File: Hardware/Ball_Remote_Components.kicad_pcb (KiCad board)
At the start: 4 copper layers, 75 x 75 mm, 55 parts, among them J1 I2C_Gyro_Module, J2 USB_B_Micro, J3 SWD_Header, Q1 SI2333DS, SW1 SW_SPDT, U1 MCP73831-2-OT, U2 L3GD20, U3 STM32WB35, U4 LD3985M28R_SOT23, Y1 32MHz, Y2 32.768MHz

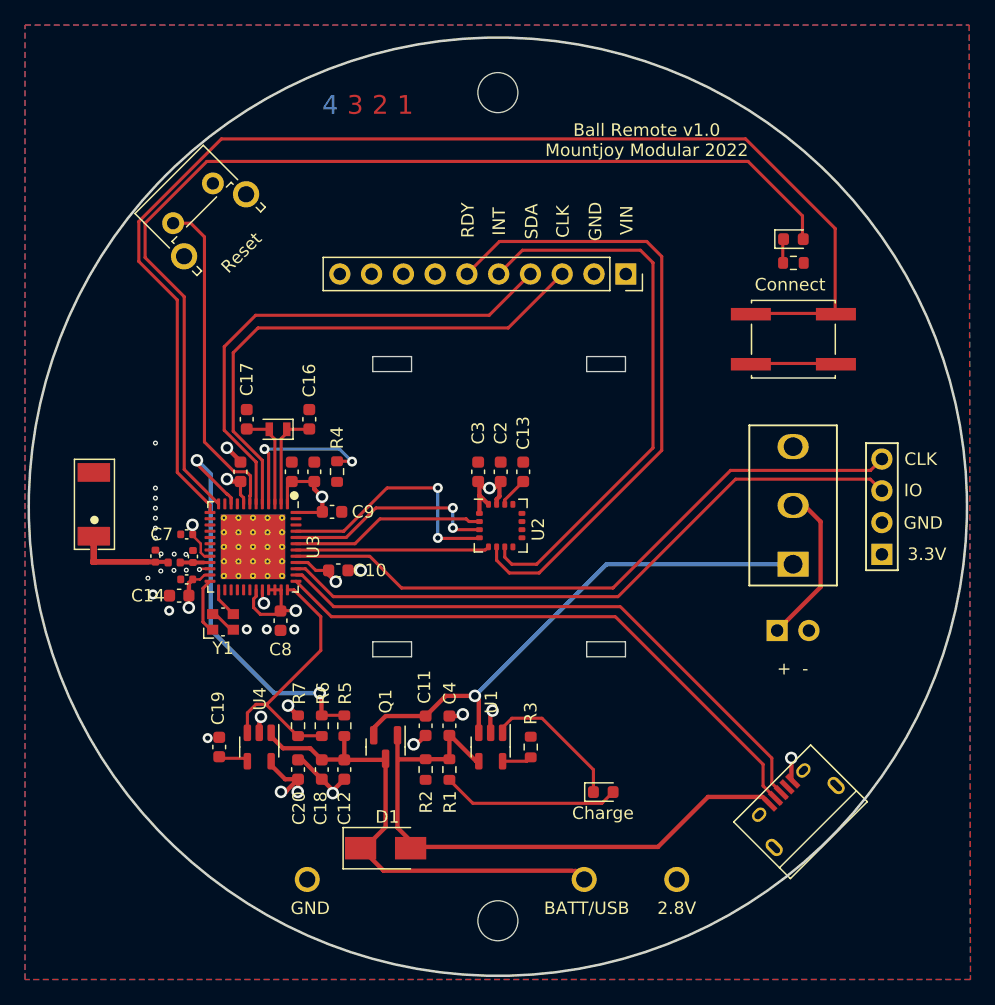
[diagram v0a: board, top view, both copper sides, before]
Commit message: More PCB clean-up
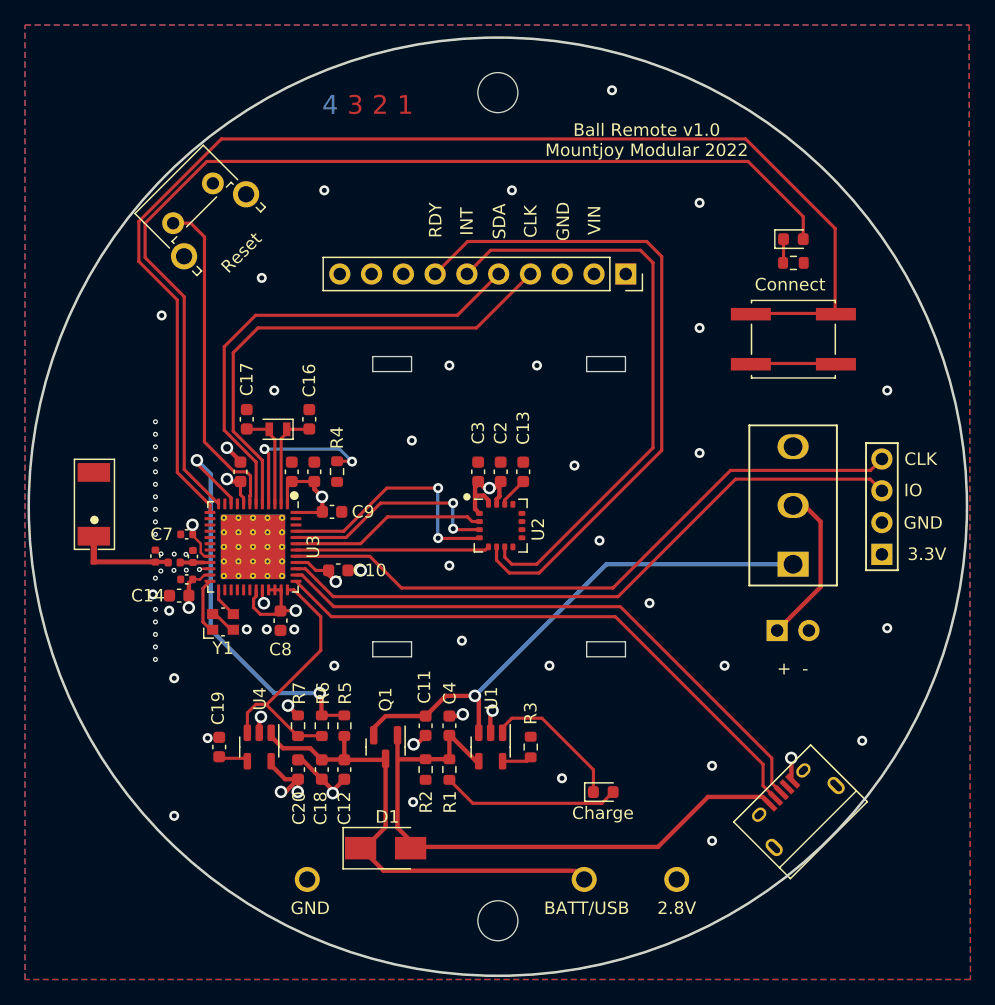
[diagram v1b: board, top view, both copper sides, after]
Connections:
- J1 pad 1: +2V8 -> unconnected-(J1-Pad1)
- J1 pad 2: GND -> +2V8
- J1 pad 3: /I2C_CLK -> GND
- J1 pad 4: /12C_SDA -> /I2C_CLK
- J1 pad 5: /G_INT -> /12C_SDA
- J1 pad 6: /G_RDY -> /G_INT
- J1 pad 7: unconnected-(J1-Pad7) -> /G_RDY
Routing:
- net /I2C_CLK: track 41.9 -> 39.4 mm
- net /12C_SDA: track 40.5 -> 38.0 mm
- net /G_RDY: track 51.4 -> 53.9 mm
- net /G_INT: track 45.1 -> 47.6 mm
- net +2V8: track 43.8 -> 44.7 mm
- net /SPI_MISO: track 17.2 -> 17.9 mm
- net GND: vias 31 -> 68

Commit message: Preparation of Gerbers for manufacturing
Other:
- board text added: "Off"
- board text added: "On"
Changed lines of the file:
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@@
     (40 "Dwgs.User" user "User.Drawings")
     (41 "Cmts.User" user "User.Comments")
-    (42 "Eco1.User" user "User.Eco1")
-    (43 "Eco2.User" user "User.Eco2")
     (44 "Edge.Cuts" user)
     (45 "Margin" user)
@@
     (48 "B.Fab" user)
     (49 "F.Fab" user)
-    (50 "User.1" user)
-    (51 "User.2" user)
-    (52 "User.3" user)
-    (53 "User.4" user)
-    (54 "User.5" user)
-    (55 "User.6" user)
-    (56 "User.7" user)
-    (57 "User.8" user)
-    (58 "User.9" user)
   )
   (setup
@@
       (drillshape 0)
       (scaleselection 1)
-      (outputdirectory "Gerbers/Remote/")
+      (outputdirectory "Gerbers/Ball_Remote/")
     )
   )
@@
       (effects (font (size 0.5 0.5) (thickness 0.1)))
     )
+    (fp_line (start -1.7 -3.5) (end 11.1 -3.5) (layer "F.SilkS") (width 0.15))
     (fp_line (start -1.7 3.5) (end 11.1 3.5) (layer "F.SilkS") (width 0.15))
     (fp_line (start 11.1 -3.5) (end 11.1 3.5) (layer "F.SilkS") (width 0.15))
-    (fp_line (start -1.7 -3.5) (end 11.1 -3.5) (layer "F.SilkS") (width 0.15))
     (fp_line (start -1.7 -3.5) (end -1.7 3.5) (layer "F.SilkS") (width 0.15))
-    (fp_line (start 11.1 -3.5) (end 11.1 3.5) (layer "F.CrtYd") (width 0.05))
     (fp_line (start -1.7 -3.5) (end 11.1 -3.5) (layer "F.CrtYd") (width 0.05))
     (fp_line (start -1.7 3.5) (end -1.7 -3.5) (layer "F.CrtYd") (width 0.05))
+    (fp_line (start 11.1 -3.5) (end 11.1 3.5) (layer "F.CrtYd") (width 0.05))
     (fp_line (start 11.1 3.5) (end -1.7 3.5) (layer "F.CrtYd") (width 0.05))
     (fp_line (start -1.7 -3.5) (end 11.1 -3.5) (layer "F.Fab") (width 0.1))
@@
   (gr_circle (center 143.4 104.5) (end 143.623607 104.5) (layer "F.SilkS") (width 0.15) (fill solid))
   (gr_circle (center 129.6 104.4) (end 129.882843 104.4) (layer "F.SilkS") (width 0.15) (fill solid))
+  (gr_rect (start 157.1 114.6) (end 160.9 95.5) (layer "F.SilkS") (width 0.15) (fill none))
   (gr_rect (start 131.925 85.2875) (end 157.425 87.9875) (layer "Dwgs.User") (width 0.15) (fill none))
   (gr_rect (start 161.975 95.2875) (end 129.975 115.2875) (layer "Dwgs.User") (width 0.15) (fill none))
@@
     (effects (font (size 1 1) (thickness 0.15)) (justify mirror))
   )
-  (gr_text "Ball Remote v1.0\nMountjoy Modular 2022" (at 157.775 75.9875) (layer "F.SilkS")
+  (gr_text "Ball Remote v1.0\nMountjoy Modular 2022" (at 158.9 105.2 90) (layer "F.SilkS")
+    (effects (font (size 1 1) (thickness 0.15)))
+  )
+  (gr_text "Off" (at 163.9 100.51) (layer "F.SilkS")
     (effects (font (size 1 1) (thickness 0.15)))
   )
@@
     (effects (font (size 1 1) (thickness 0.15)))
   )
+  (gr_text "On" (at 163.8 109.87) (layer "F.SilkS")
+    (effects (font (size 1 1) (thickness 0.15)))
+  )

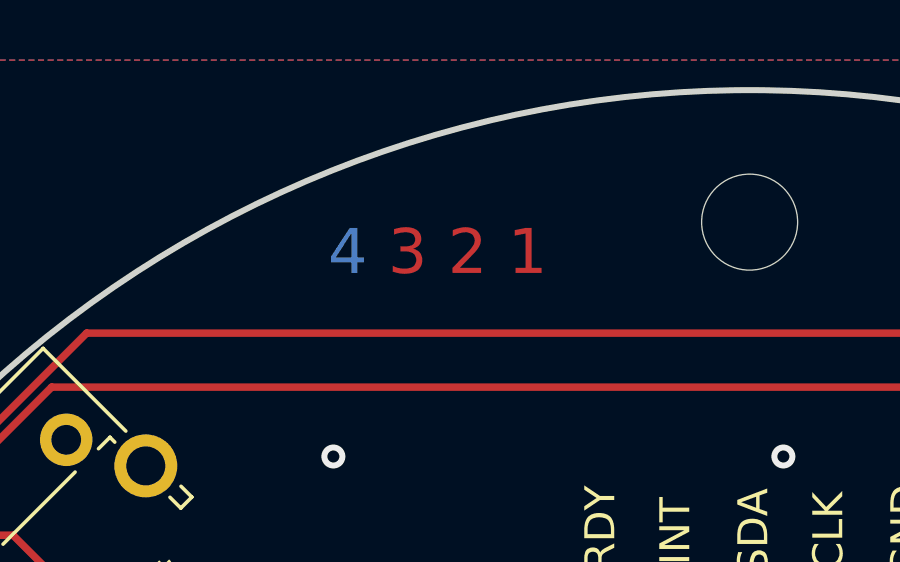
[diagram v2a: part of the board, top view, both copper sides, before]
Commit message: Fixed 4-layer marker incorrect copper layers
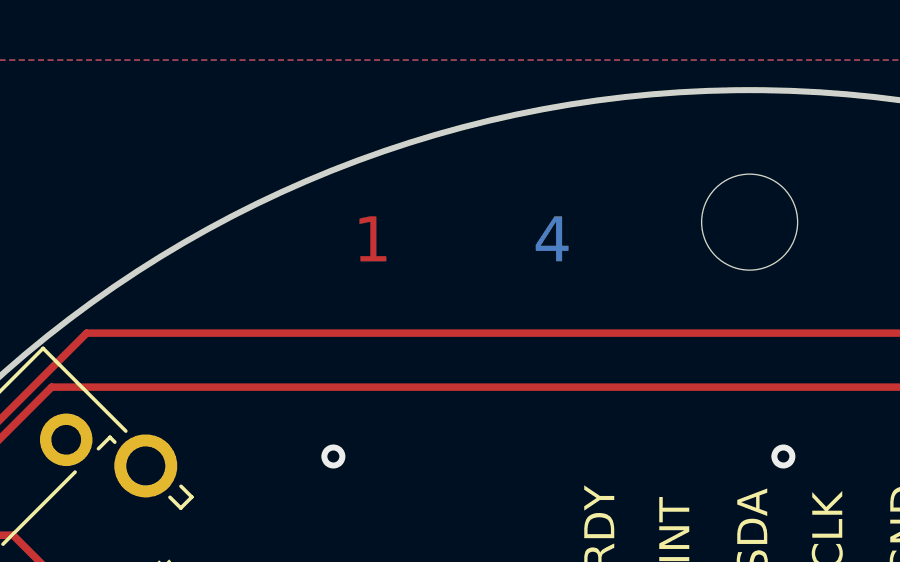
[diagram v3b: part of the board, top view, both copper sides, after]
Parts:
- moved FID1 0.91 mm to (136.3, 72.8), turned to 0 degrees
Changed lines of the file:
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@@
+    )
+  )
+  (footprint "Custom_Footprints:4_Layer_Markers" (layer "F.Cu")
+    (at 136.3 72.8)
+    (property "Sheetfile" "Ball_Remote_Components.kicad_sch")
+    (property "Sheetname" "")
+    (attr through_hole)
+    (fp_text reference "FID1" (at 0 4) (layer "F.SilkS") hide
+      (effects (font (size 1 1) (thickness 0.15)))
+    )
+    (fp_text value "4 Layer Marker" (at 0 -4) (layer "F.Fab")
+      (effects (font (size 1 1) (thickness 0.15)))
+    )
+    (fp_text user "1" (at -3 0) (layer "F.Cu")
+      (effects (font (size 1.5 1.5) (thickness 0.3)))
+    )
+    (fp_text user "2" (at -1 0) (layer "In1.Cu")
+      (effects (font (size 1.5 1.5) (thickness 0.3)))
+    )
+    (fp_text user "3" (at 1 0) (layer "In2.Cu")
+      (effects (font (size 1.5 1.5) (thickness 0.3)))
+    )
+    (fp_text user "4" (at 3 0) (layer "B.Cu")
+      (effects (font (size 1.5 1.5) (thickness 0.3)))
+    )
+    (fp_poly (pts
+        (xy 4 1)
+        (xy -4 1)
+        (xy -4 -1)
+        (xy 4 -1)
+      ) (layer "B.Mask") (width 0.1) (fill solid))
+    (fp_poly (pts
+        (xy 4 1)
+        (xy -4 1)
+        (xy -4 -1)
+        (xy 4 -1)
+      ) (layer "F.Mask") (width 0.1) (fill solid))
+    (zone (net 0) (net_name "") (layers *.Cu) (hatch edge 0.508)
+      (connect_pads (clearance 0))
+      (min_thickness 0.254)
+      (keepout (tracks not_allowed) (vias not_allowed) (pads not_allowed ) (copperpour not_allowed) (footprints allowed))
+      (fill (thermal_gap 0.508) (thermal_bridge_width 0.508))
+      (polygon
+        (pts
+          (xy 140.4 73.9)
+          (xy 132.2 73.9)
+          (xy 132.2 71.7)
+          (xy 140.4 71.7)
+        )
+      )
     )
   )
@@
     )
   )
-  (footprint "Custom_Footprints:4_Layer_Markers" (layer "F.Cu")
-    (at 135.475 73.1875 180)
-    (property "Sheetfile" "Ball_Remote_Components.kicad_sch")
-    (property "Sheetname" "")
-    (attr through_hole)
-    (fp_text reference "FID1" (at 0 4) (layer "F.SilkS") hide
-      (effects (font (size 1 1) (thickness 0.15)))
-    )
-    (fp_text value "4 Layer Marker" (at 0 -4) (layer "F.Fab")
-      (effects (font (size 1 1) (thickness 0.15)))
-    )
-    (fp_text user "1" (at -3 0) (layer "F.Cu")
-      (effects (font (size 1.5 1.5) (thickness 0.3)))
-    )
-    (fp_text user "3" (at 1 0) (layer "F.Cu")
-      (effects (font (size 1.5 1.5) (thickness 0.3)))
-    )
-    (fp_text user "2" (at -1 0) (layer "F.Cu")
-      (effects (font (size 1.5 1.5) (thickness 0.3)))
-    )
-    (fp_text user "4" (at 3 0) (layer "B.Cu")
-      (effects (font (size 1.5 1.5) (thickness 0.3)))
-    )
-    (fp_poly (pts
-        (xy 4 1)
-        (xy -4 1)
-        (xy -4 -1)
-        (xy 4 -1)
-      ) (layer "B.Mask") (width 0.1) (fill solid))
-    (fp_poly (pts
-        (xy 4 1)
-        (xy -4 1)
-        (xy -4 -1)
-        (xy 4 -1)
-      ) (layer "F.Mask") (width 0.1) (fill solid))
-    (zone (net 0) (net_name "") (layers *.Cu) (hatch edge 0.508)
-      (connect_pads (clearance 0))
-      (min_thickness 0.254)
-      (keepout (tracks not_allowed) (vias not_allowed) (pads not_allowed ) (copperpour not_allowed) (footprints allowed))
-      (fill (thermal_gap 0.508) (thermal_bridge_width 0.508))
-      (polygon
-        (pts
-          (xy 131.375 72.0875)
-          (xy 139.575 72.0875)
-          (xy 139.575 74.2875)
-          (xy 131.375 74.2875)
-        )
-      )
-    )
-  )

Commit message: Created test firmware for STM32WB35 hardware (not yet working)
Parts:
- C16, C17: value 16pF -> 20pF
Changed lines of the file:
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@@
       (effects (font (size 1 1) (thickness 0.15)))
     )
-    (fp_text value "16pF" (at 0 1.43 90) (layer "F.Fab")
+    (fp_text value "20pF" (at 0 1.43 90) (layer "F.Fab")
       (effects (font (size 1 1) (thickness 0.15)))
     )
@@
       (effects (font (size 1 1) (thickness 0.15)))
     )
-    (fp_text value "16pF" (at 0 1.43 -270) (layer "F.Fab")
+    (fp_text value "20pF" (at 0 1.43 -270) (layer "F.Fab")
       (effects (font (size 1 1) (thickness 0.15)))
     )

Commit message: More library files updated
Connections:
- net /LED_BLUE_OUT renamed /Led_Connect

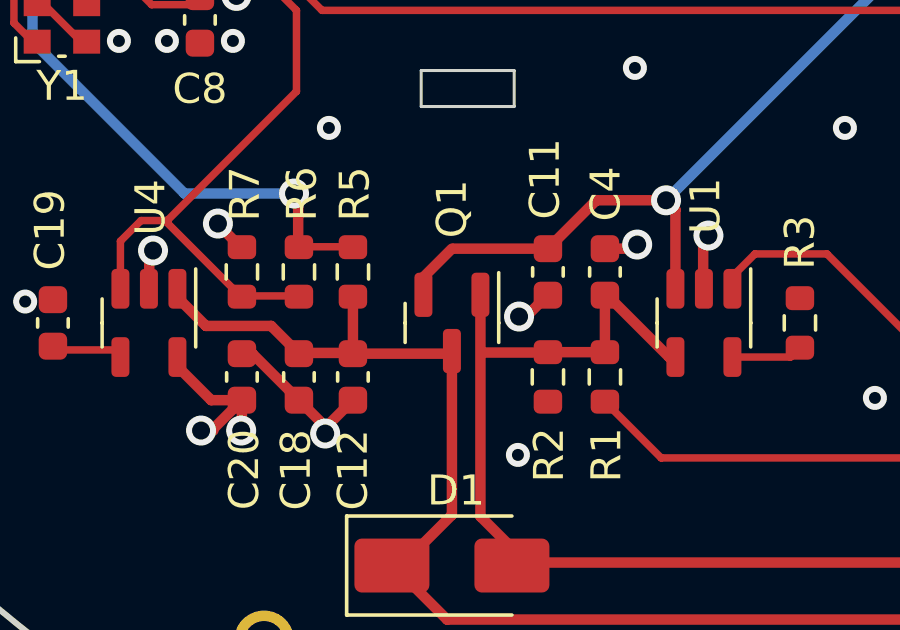
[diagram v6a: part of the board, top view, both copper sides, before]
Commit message: Base will periodically wake up remote to check battery level and flash if battery low
Removed offsets from base as handled in remote
Added config for battery warnings and sensitivity
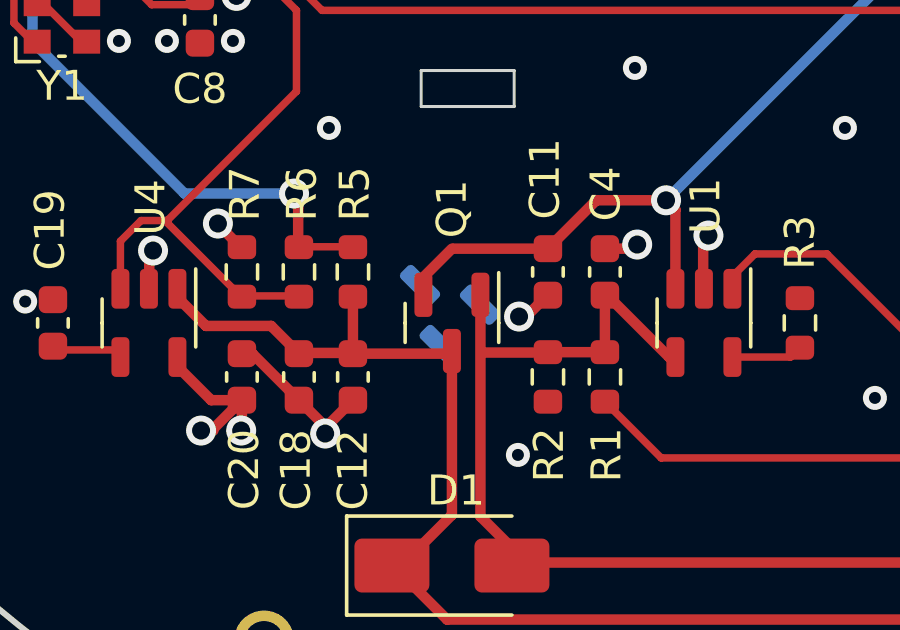
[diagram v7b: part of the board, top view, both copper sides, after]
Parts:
- added Q1: SI2333DS, Package_TO_SOT_SMD:SOT-23, B.Cu at (136.5, 123.9)
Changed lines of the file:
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@@
+    )
+  )
+  (footprint "Package_TO_SOT_SMD:SOT-23" (layer "B.Cu")
+    (at 136.5 123.9 135)
+    (descr "SOT, 3 Pin (https://www.jedec.org/system/files/docs/to-236h.pdf variant AB), generated with kicad-footprint-generator ipc_gullwing_generator.py")
+    (tags "SOT TO_SOT_SMD")
+    (property "Sheetfile" "Ball_Remote_Components.kicad_sch")
+    (property "Sheetname" "")
+    (property "ki_description" "-4.4A Id, -40V Vds, P-Channel MOSFET, SOT-23")
+    (property "ki_keywords" "P-Channel MOSFET")
+    (attr smd)
+    (fp_text reference "Q1" (at -3.8 0 135) (layer "B.SilkS")
+        (effects (font (size 1 1) (thickness 0.15)) (justify mirror))
+    )
+    (fp_text value "SI2333DS" (at 0 -2.4 135) (layer "B.Fab")
+        (effects (font (size 1 1) (thickness 0.15)) (justify mirror))
+    )
+    (fp_text user "${REFERENCE}" (at 0 0 135) (layer "B.Fab")
+        (effects (font (size 0.32 0.32) (thickness 0.05)) (justify mirror))
+    )
+    (fp_line (start 0 -1.56) (end -0.65 -1.56)
+      (stroke (width 0.12) (type solid)) (layer "B.SilkS"))
+    (fp_line (start 0 -1.56) (end 0.65 -1.56)
+      (stroke (width 0.12) (type solid)) (layer "B.SilkS"))
+    (fp_line (start 0 1.56) (end -1.675 1.56)
+      (stroke (width 0.12) (type solid)) (layer "B.SilkS"))
+    (fp_line (start 0 1.56) (end 0.65 1.56)
+      (stroke (width 0.12) (type solid)) (layer "B.SilkS"))
+    (fp_line (start -1.92 -1.7) (end 1.92 -1.7)
+      (stroke (width 0.05) (type solid)) (layer "B.CrtYd"))
+    (fp_line (start -1.92 1.7) (end -1.92 -1.7)
+      (stroke (width 0.05) (type solid)) (layer "B.CrtYd"))
+    (fp_line (start 1.92 -1.7) (end 1.92 1.7)
+      (stroke (width 0.05) (type solid)) (layer "B.CrtYd"))
+    (fp_line (start 1.92 1.7) (end -1.92 1.7)
+      (stroke (width 0.05) (type solid)) (layer "B.CrtYd"))
+    (fp_line (start -0.65 -1.45) (end -0.65 1.125)
+      (stroke (width 0.1) (type solid)) (layer "B.Fab"))
+    (fp_line (start -0.65 1.125) (end -0.325 1.45)
+      (stroke (width 0.1) (type solid)) (layer "B.Fab"))
+    (fp_line (start -0.325 1.45) (end 0.65 1.45)
+      (stroke (width 0.1) (type solid)) (layer "B.Fab"))
+    (fp_line (start 0.65 -1.45) (end -0.65 -1.45)
+      (stroke (width 0.1) (type solid)) (layer "B.Fab"))
+    (fp_line (start 0.65 1.45) (end 0.65 -1.45)
+      (stroke (width 0.1) (type solid)) (layer "B.Fab"))
+    (pad "1" smd roundrect (at -0.9375 0.95 135) (size 1.475 0.6) (layers "B.Cu" "B.Paste" "B.Mask") (roundrect_rratio 0.25)
+      (pinfunction "G") (pintype "input"))
+    (pad "2" smd roundrect (at -0.9375 -0.95 135) (size 1.475 0.6) (layers "B.Cu" "B.Paste" "B.Mask") (roundrect_rratio 0.25)
+      (pinfunction "S") (pintype "passive"))
+    (pad "3" smd roundrect (at 0.9375 0 135) (size 1.475 0.6) (layers "B.Cu" "B.Paste" "B.Mask") (roundrect_rratio 0.25)
+      (pinfunction "D") (pintype "passive"))
+    (model "${KICAD6_3DMODEL_DIR}/Package_TO_SOT_SMD.3dshapes/SOT-23.wrl"
+      (offset (xyz 0 0 0))
+      (scale (xyz 1 1 1))
+      (rotate (xyz 0 0 0))
     )
   )
